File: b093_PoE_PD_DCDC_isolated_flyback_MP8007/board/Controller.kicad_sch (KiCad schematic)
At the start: 19 parts, among them U1 MP8007, U2 CX9628-AL

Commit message: version 0.3
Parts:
- added C10: 1nF, Capacitor_SMD:C_1825_4564Metric, symbol Device:C_Small
- added C5: 1nF, Capacitor_SMD:C_0603_1608Metric, symbol Device:C_Small
- added C9: 10n, Capacitor_SMD:C_0805_2012Metric, symbol Device:C
- added D3: BAV21, Diode_SMD:D_SOD-323_HandSoldering, symbol Device:D
- added R8: 10K, Resistor_SMD:R_1206_3216Metric, symbol Device:R
- L1: value L_Small -> 0R
- U2: value CX9628-AL -> POE70P-12L; footprint (none) -> local:Transformer_Coilcraft_POE70P; symbol local:CX9628-AL -> local:POE70P-50L
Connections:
- net GNDPWR: now also U2.1 (B-), C10.1; no longer U2.4 (B-)
- net PoE+: no longer C3.1, C4.1
- net at U1.12 (SW), U1.13, U2.3 (P+): now also D3.2 (A)
- net at R7.2: now also C5.2
- net at L1.2: now also C3.1, C4.1, U2.4 (P-), C9.1, R8.2; no longer U2.1 (P-)
- net at D1.2 (A), R6.1: now also U2.2 (B+); no longer U2.5 (B+)
- net at D2.2 (A), U2.6 (S+): now also U2.5 (S2+), C5.1; no longer U2.7 (S+)
- net GNDA renamed GND
- net GND: now also U2.7 (S2-), U2.8 (S-), C10.2; no longer U2.10 (S-), U2.9 (S2-)
- new net: C9.2, D3.1 (K), R8.1
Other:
- moved on the sheet: C3, C4, D1, L1, R1, R2, R6

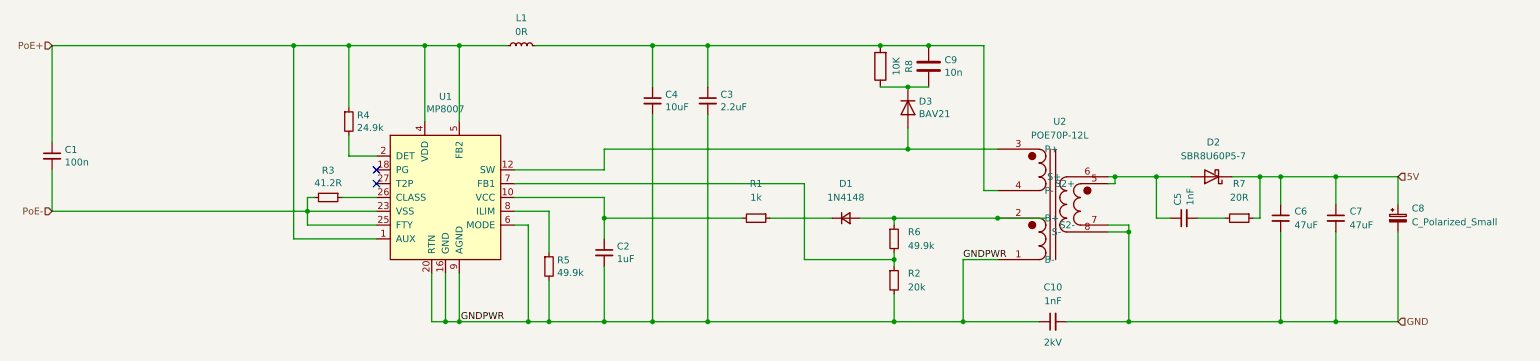
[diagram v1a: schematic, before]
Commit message: increased board size and updated component values
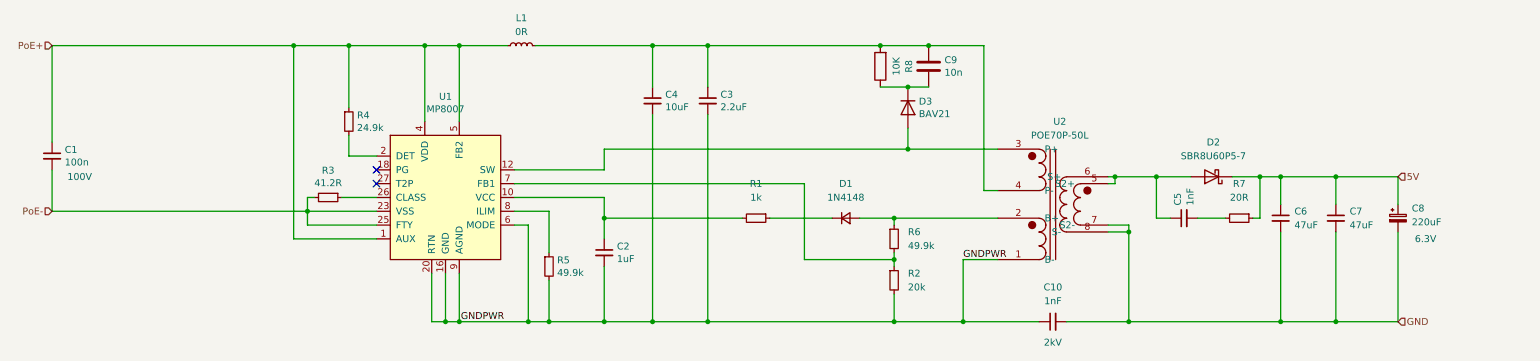
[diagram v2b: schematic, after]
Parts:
- C1: Voltage (none) -> 100V
- C8: value C_Polarized_Small -> 220uF; footprint (none) -> Capacitor_SMD:CP_Elec_10x10.5; Voltage (none) -> 6.3V
- D1: DigiKey_PN (none) -> 1N4148WS_R1_00001
- L1: footprint (none) -> Inductor_SMD:L_1812_4532Metric
- U2: value POE70P-12L -> POE70P-50L
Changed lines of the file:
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@@
   (junction (at 187.96 81.28) (diameter 0) (color 0 0 0 0)
-  )
-  (junction (at 204.47 93.98) (diameter 0) (color 0 0 0 0)
   )
   (junction (at 99.06 62.23) (diameter 0) (color 0 0 0 0)
@@
   )
   (wire (pts (xy 121.92 105.41) (xy 121.92 113.03))
-    (stroke (width 0) (type default) (color 0 0 0 0))
-  )
-  (wire (pts (xy 213.36 93.98) (xy 204.47 93.98))
     (stroke (width 0) (type default) (color 0 0 0 0))
   )
@@
       (effects (font (size 1.27 1.27)) hide)
     )
+    (property "Voltage" "100V" (id 4) (at 35.56 86.36 0))
     (pin "1")
     (pin "2")
@@
   )
   (symbol (lib_id "Device:C_Polarized_Small") (at 278.13 93.98 0) (unit 1)
-    (in_bom yes) (on_board yes) (fields_autoplaced)
+    (in_bom yes) (on_board yes)
     (property "Reference" "C8" (id 0) (at 280.67 92.1638 0)
       (effects (font (size 1.27 1.27)) (justify left))
     )
-    (property "Value" "C_Polarized_Small" (id 1) (at 280.67 94.7038 0)
-      (effects (font (size 1.27 1.27)) (justify left))
-    )
-    (property "Footprint" "" (id 2) (at 278.13 93.98 0)
+    (property "Value" "220uF" (id 1) (at 280.67 94.7038 0)
+      (effects (font (size 1.27 1.27)) (justify left))
+    )
+    (property "Footprint" "Capacitor_SMD:CP_Elec_10x10.5" (id 2) (at 278.13 93.98 0)
       (effects (font (size 1.27 1.27)) hide)
     )
@@
       (effects (font (size 1.27 1.27)) hide)
     )
+    (property "Voltage" "6.3V" (id 4) (at 283.21 97.79 0))
     (pin "1")
     (pin "2")
@@
     (property "Reference" "L1" (id 0) (at 116.84 57.15 90))
     (property "Value" "0R" (id 1) (at 116.84 59.69 90))
-    (property "Footprint" "" (id 2) (at 116.84 62.23 0)
+    (property "Footprint" "Inductor_SMD:L_1812_4532Metric" (id 2) (at 116.84 62.23 0)
       (effects (font (size 1.27 1.27)) hide)
     )
@@
       (effects (font (size 1.27 1.27)) hide)
     )
+    (property "DigiKey_PN" "1N4148WS_R1_00001" (id 4) (at 176.53 93.98 0)
+      (effects (font (size 1.27 1.27)) hide)
+    )
     (pin "1")
     (pin "2")
@@
     (in_bom yes) (on_board yes) (fields_autoplaced)
     (property "Reference" "U2" (id 0) (at 215.9 76.2 0))
-    (property "Value" "POE70P-12L" (id 1) (at 215.9 78.74 0))
+    (property "Value" "POE70P-50L" (id 1) (at 215.9 78.74 0))
     (property "Footprint" "local:Transformer_Coilcraft_POE70P" (id 2) (at 214.63 91.44 0)
       (effects (font (size 1.27 1.27)) hide)

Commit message: improved component constraints
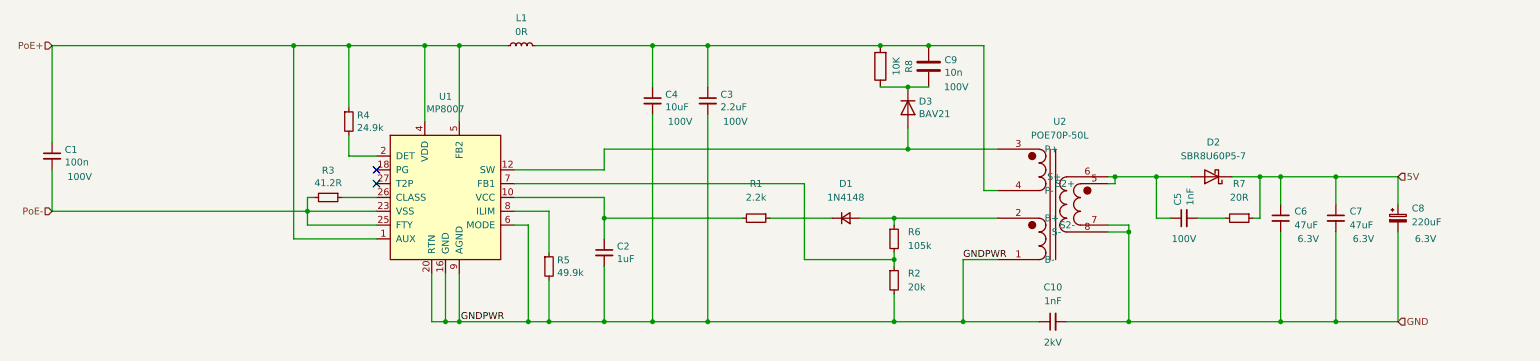
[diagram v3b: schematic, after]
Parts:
- C3, C4: Voltage (none) -> 100V
- C5: MPN (none) -> GRM188R72A102KA01D; TC (none) -> X7R; Voltage (none) -> 100V
- C6, C7: Voltage (none) -> 6.3V
- C9: MPN (none) -> GRM216R72A103KA01D; TC (none) -> X7R; Voltage (none) -> 100V
- R1: value 1k -> 2.2k
- R6: value 49.9k -> 105k
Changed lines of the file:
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@@
       (effects (font (size 1.27 1.27)) hide)
     )
+    (property "Voltage" "100V" (id 4) (at 156.21 76.2 0))
     (pin "1")
     (pin "2")
@@
       (effects (font (size 1.27 1.27)) hide)
     )
+    (property "Voltage" "100V" (id 4) (at 146.05 76.2 0))
     (pin "1")
     (pin "2")
@@
     (in_bom yes) (on_board yes) (fields_autoplaced)
     (property "Reference" "R1" (id 0) (at 160.02 87.63 90))
-    (property "Value" "1k" (id 1) (at 160.02 90.17 90))
+    (property "Value" "2.2k" (id 1) (at 160.02 90.17 90))
     (property "Footprint" "Resistor_SMD:R_0603_1608Metric" (id 2) (at 160.02 93.98 0)
       (effects (font (size 1.27 1.27)) hide)
@@
       (effects (font (size 1.27 1.27)) hide)
     )
+    (property "MPN" "GRM188R72A102KA01D" (id 4) (at 238.76 93.98 0)
+      (effects (font (size 1.27 1.27)) hide)
+    )
+    (property "Voltage" "100V" (id 5) (at 238.76 97.79 90))
+    (property "TC" "X7R" (id 6) (at 238.76 93.98 0)
+      (effects (font (size 1.27 1.27)) hide)
+    )
     (pin "1")
     (pin "2")
@@
       (effects (font (size 1.27 1.27)) hide)
     )
+    (property "Voltage" "100V" (id 4) (at 196.85 69.85 0))
+    (property "TC" "X7R" (id 5) (at 191.77 66.04 0)
+      (effects (font (size 1.27 1.27)) hide)
+    )
+    (property "MPN" "GRM216R72A103KA01D" (id 6) (at 191.77 66.04 0)
+      (effects (font (size 1.27 1.27)) hide)
+    )
     (pin "1")
     (pin "2")
   )
   (symbol (lib_id "Device:C_Small") (at 266.7 93.98 0) (unit 1)
-    (in_bom yes) (on_board yes) (fields_autoplaced)
+    (in_bom yes) (on_board yes)
     (property "Reference" "C7" (id 0) (at 269.24 92.7162 0)
       (effects (font (size 1.27 1.27)) (justify left))
@@
       (effects (font (size 1.27 1.27)) hide)
     )
+    (property "Voltage" "6.3V" (id 4) (at 271.78 97.79 0))
     (pin "1")
     (pin "2")
@@
       (effects (font (size 1.27 1.27)) (justify left))
     )
-    (property "Value" "49.9k" (id 1) (at 187.96 99.0599 0)
+    (property "Value" "105k" (id 1) (at 187.96 99.0599 0)
       (effects (font (size 1.27 1.27)) (justify left))
     )
@@
   )
   (symbol (lib_id "Device:C_Small") (at 256.54 93.98 0) (unit 1)
-    (in_bom yes) (on_board yes) (fields_autoplaced)
+    (in_bom yes) (on_board yes)
     (property "Reference" "C6" (id 0) (at 259.08 92.7162 0)
       (effects (font (size 1.27 1.27)) (justify left))
@@
       (effects (font (size 1.27 1.27)) hide)
     )
-    (pin "1")
-    (pin "2")
+    (property "Voltage" "6.3V" (id 4) (at 261.62 97.79 0))
+    (pin "1")
+    (pin "2")
